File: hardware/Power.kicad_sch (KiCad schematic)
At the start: 43 parts, among them SW8 GT-TC054A-H035-L1, U10 SGM6603-ADJYN6G, U11 SGM3204, U9 AXP2101

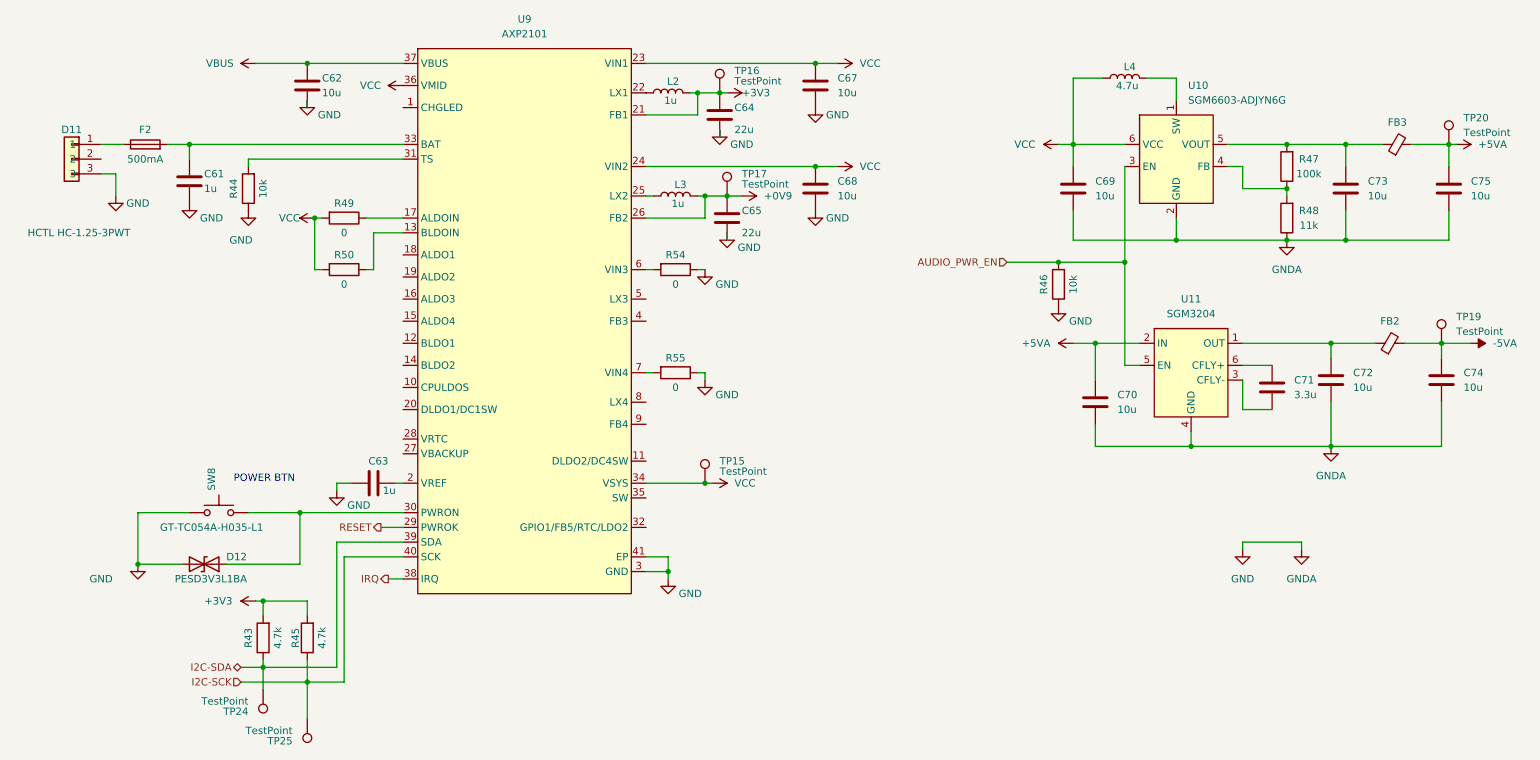
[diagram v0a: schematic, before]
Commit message: some changes on fab layers
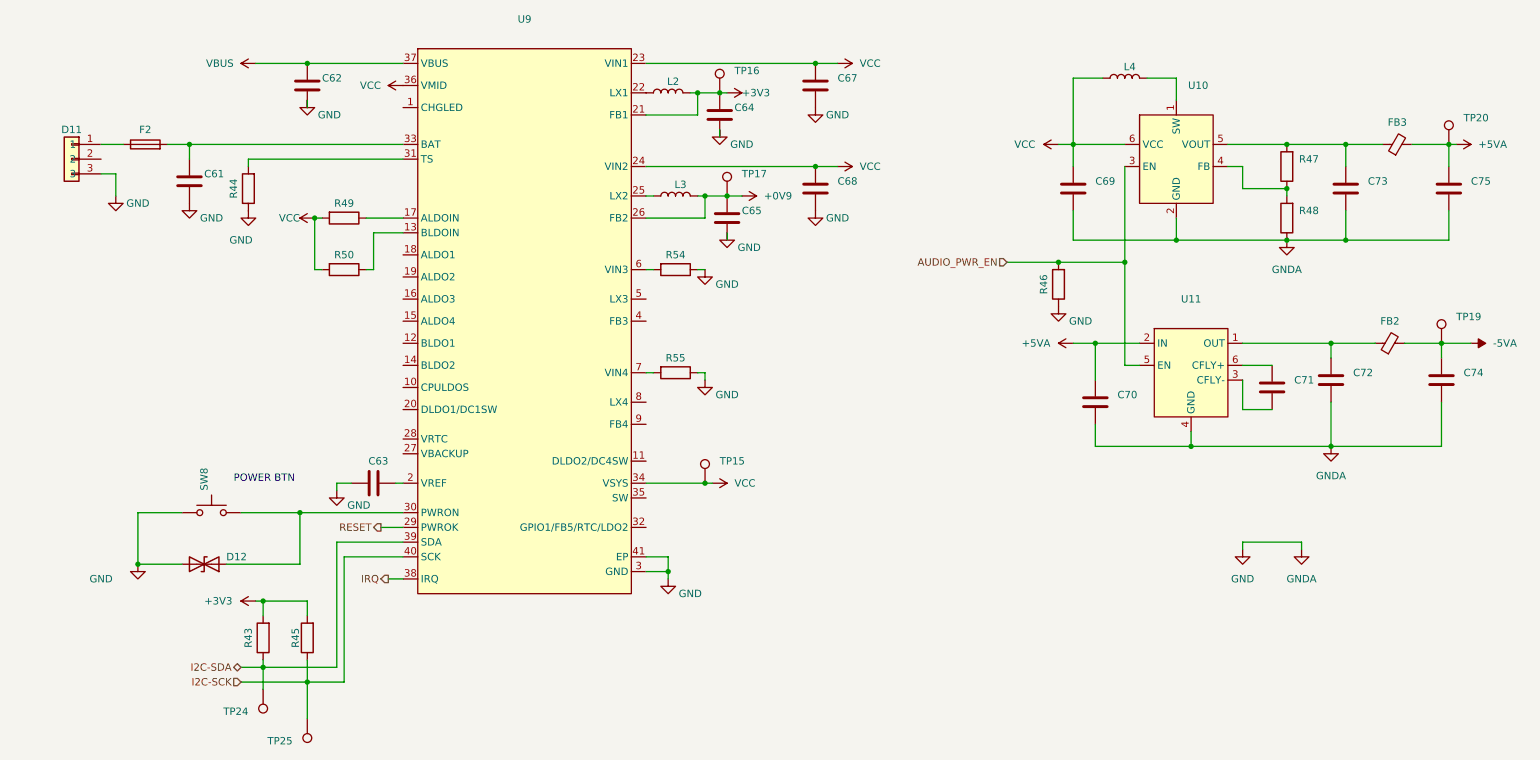
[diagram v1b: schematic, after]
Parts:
- C61, C63: value 1u -> (none); footprint rlib_passive:C_0603_1608Metric -> (none)
- C62, C67, C68, C69, C70, C72, C73, C74, C75: value 10u -> (none); footprint rlib_passive:C_0603_1608Metric -> (none)
- C64, C65: value 22u -> (none); footprint rlib_passive:C_0603_1608Metric -> (none)
- C71: value 3.3u -> (none); footprint rlib_passive:C_0603_1608Metric -> (none)
- D11: value HCTL HC-1.25-3PWT -> (none); footprint rlib_connectors:CONN-SMD_HC-1.25-3PWT -> (none)
- D12: value PESD3V3L1BA -> (none); footprint rlib_passive:D_SOD-323F -> (none)
- F2: value 500mA -> (none); footprint rlib_passive:FUSC3216X85N -> (none)
- FB2, FB3: value FerriteBead -> (none); footprint rlib_passive:INDC2520X120N -> (none)
- L2, L3: value 1u -> (none); footprint rlib_passive:INDC2016X100N -> (none)
- L4: value 4.7u -> (none); footprint rlib_passive:IND_LQH32PN4R7NN0L -> (none)
- R43, R45: value 4.7k -> (none); footprint rlib_passive:R_0603_1608Metric -> (none)
- R44, R46: value 10k -> (none); footprint rlib_passive:R_0603_1608Metric -> (none)
- R47: value 100k -> (none); footprint rlib_passive:R_0603_1608Metric -> (none)
- R48: value 11k -> (none); footprint rlib_passive:R_0603_1608Metric -> (none)
- R49, R50, R54, R55: value 0 -> (none); footprint rlib_passive:R_0603_1608Metric -> (none)
- SW8: value GT-TC054A-H035-L1 -> (none); footprint rlib_buttons:GT-TC054A-H035-L1 -> (none)
- TP15, TP16, TP17, TP19, TP20, TP24, TP25: value TestPoint -> (none); footprint TestPoint:TestPoint_Pad_D1.0mm -> (none)
- U10: value SGM6603-ADJYN6G -> (none); footprint rlib_power:SOT-23-6 -> (none)
- U11: value SGM3204 -> (none); footprint rlib_power:SOT-23-6 -> (none)
- U9: value AXP2101 -> (none); footprint rlib_power:QFN-40_L5.0-W5.0-P0.40-TL-EP3.4 -> (none)
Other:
- moved on the sheet: SW8

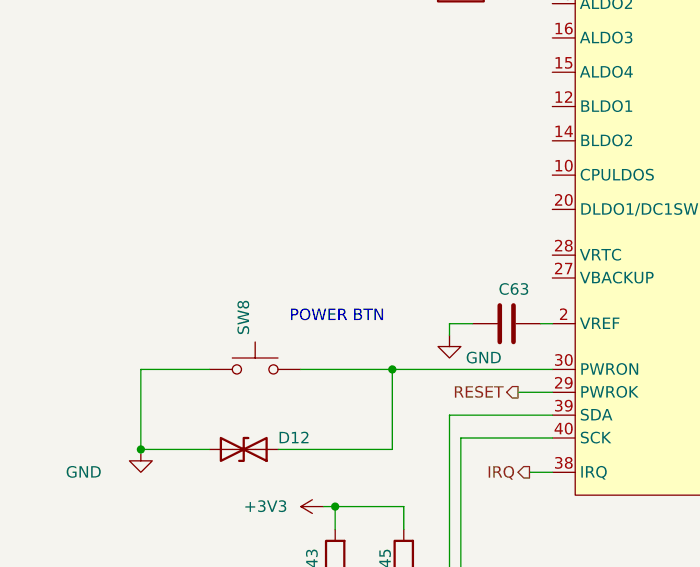
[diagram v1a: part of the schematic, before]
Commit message: pwr btn is optional connected to soc
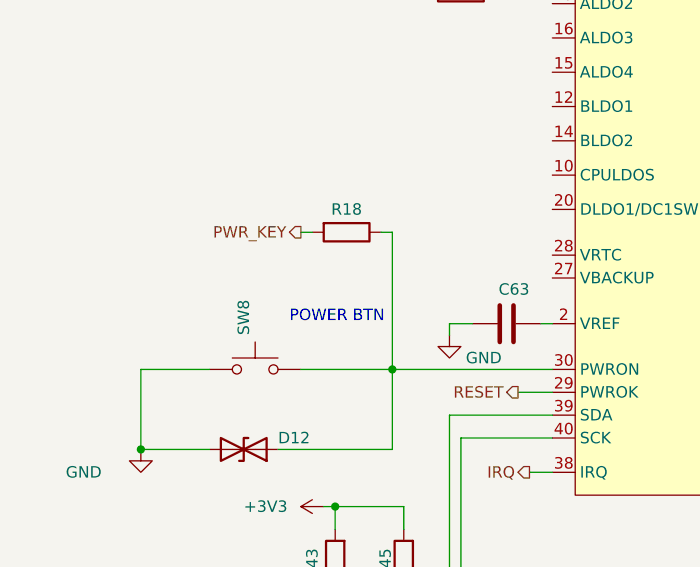
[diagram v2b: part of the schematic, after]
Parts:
- added R18: (no value), symbol rlib_passive:R
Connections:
- net at D12.1 (A1), SW8.2, U9.30 (PWRON): now also R18.1
- new net PWR_KEY: R18.2
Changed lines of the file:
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@@
+    (stroke (width 0) (type default) (color 0 0 0 0))
+  )
+  (wire (pts (xy 62.23 105.41) (xy 63.5 105.41))
     (stroke (width 0) (type default) (color 0 0 0 0))
   )
@@
     (stroke (width 0) (type default) (color 0 0 0 0))
   )
+  (wire (pts (xy 63.5 105.41) (xy 63.5 120.65))
+    (stroke (width 0) (type default) (color 0 0 0 0))
+  )
   (wire (pts (xy 132.08 48.26) (xy 132.08 52.07))
     (stroke (width 0) (type default) (color 0 0 0 0))
@@
   )
   (wire (pts (xy 214.63 49.53) (xy 214.63 45.72))
+    (stroke (width 0) (type default) (color 0 0 0 0))
+  )
+  (wire (pts (xy 53.34 105.41) (xy 54.61 105.41))
     (stroke (width 0) (type default) (color 0 0 0 0))
   )
@@
   )
   (hierarchical_label "IRQ" (shape output) (at 78.74 132.08 180)
+    (effects (font (size 1.27 1.27)) (justify right))
+  )
+  (hierarchical_label "PWR_KEY" (shape output) (at 53.34 105.41 180)
     (effects (font (size 1.27 1.27)) (justify right))
   )
@@
     (pin "1")
   )
+  (symbol (lib_id "rlib_passive:R") (at 58.42 105.41 270) (unit 1)
+    (in_bom yes) (on_board yes)
+    (property "Reference" "R18" (id 0) (at 58.42 102.87 90))
+    (property "Value" "" (id 1) (at 58.42 107.95 90))
+    (property "Footprint" "" (id 2) (at 58.42 103.632 90)
+      (effects (font (size 1.27 1.27)) hide)
+    )
+    (property "Datasheet" "~" (id 3) (at 58.42 105.41 0)
+      (effects (font (size 1.27 1.27)) hide)
+    )
+    (property "Tolerance" "" (id 4) (at 58.42 105.41 0)
+      (effects (font (size 1.27 1.27)) hide)
+    )
+    (property "Manufacturer" "Viking Tech" (id 5) (at 58.42 105.41 0)
+      (effects (font (size 1.27 1.27)) hide)
+    )
+    (property "Mnfct.  partnumber" "" (id 6) (at 58.42 105.41 0)
+      (effects (font (size 1.27 1.27)) hide)
+    )
+    (property "LCSC Partnumber" "" (id 8) (at 58.42 105.41 0)
+      (effects (font (size 1.27 1.27)) hide)
+    )
+    (property "LCSC partnumber" "C465460" (id 9) (at 58.42 105.41 0)
+      (effects (font (size 1.27 1.27)) hide)
+    )
+    (property "Mnfct. partnumber" "CR-03JA7----0R " (id 10) (at 58.42 105.41 0)
+      (effects (font (size 1.27 1.27)) hide)
+    )
+    (pin "1")
+    (pin "2")
+  )
   (symbol (lib_name "C_12") (lib_id "rlib_passive:C") (at 152.4 46.99 0) (unit 1)

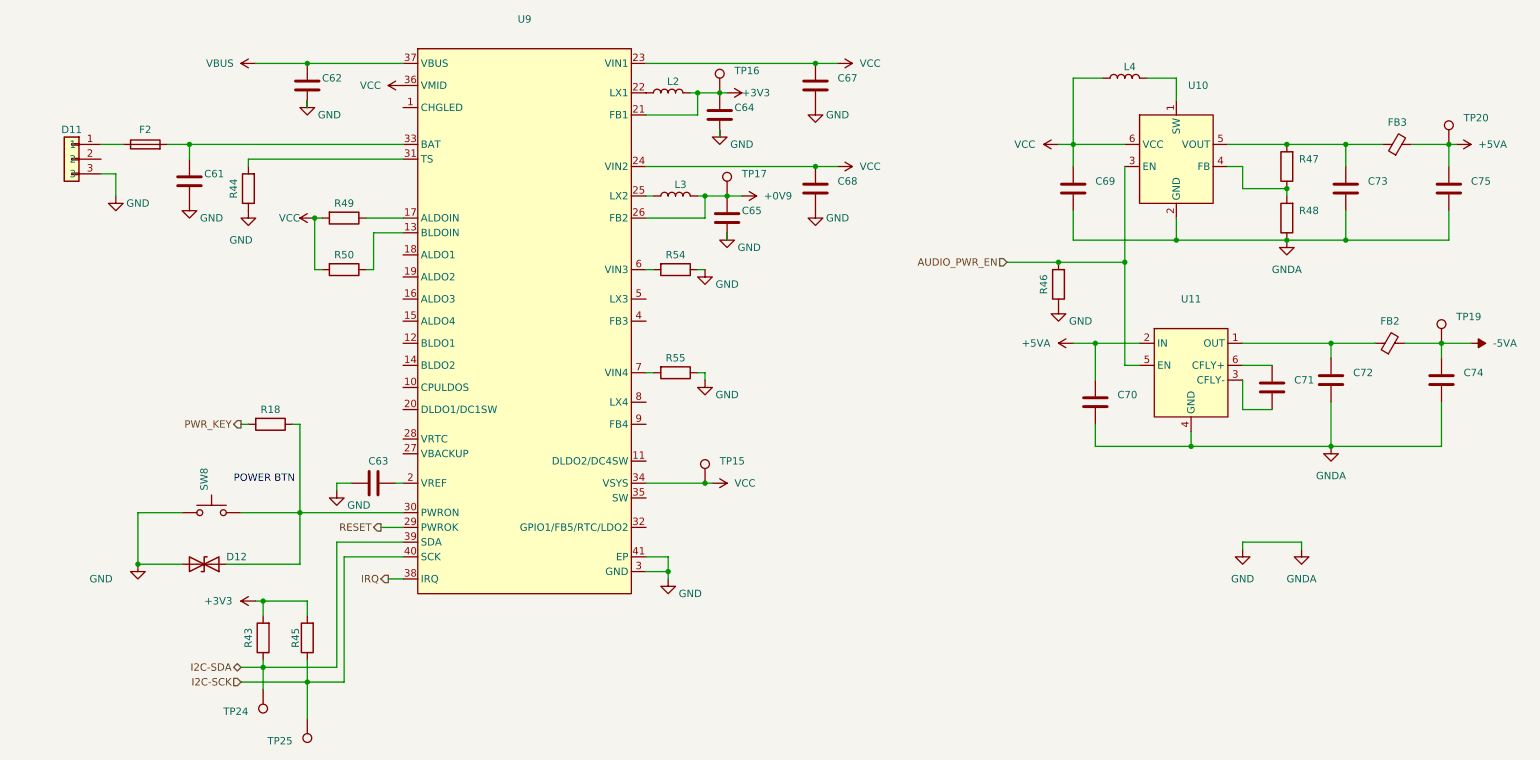
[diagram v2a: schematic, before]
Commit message: ferrite bead in adc power net is added
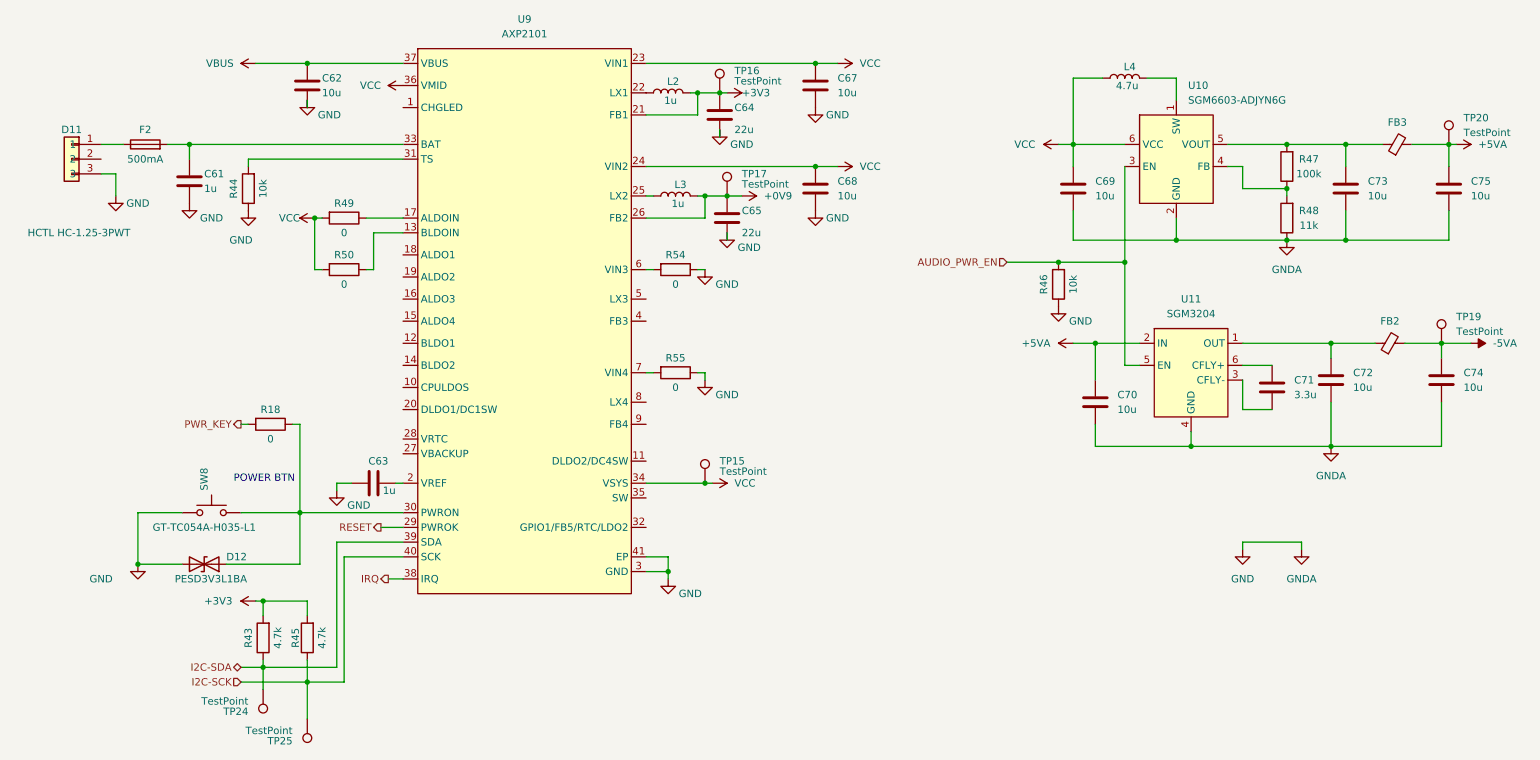
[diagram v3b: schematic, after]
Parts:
- C61, C63, L2, L3: value (none) -> 1u
- C62, C67, C68, C69, C70, C72, C73, C74, C75: value (none) -> 10u
- C64, C65: value (none) -> 22u
- C71: value (none) -> 3.3u
- D11: value (none) -> HCTL HC-1.25-3PWT
- D12: value (none) -> PESD3V3L1BA
- F2: value (none) -> 500mA
- L4: value (none) -> 4.7u
- R18, R49, R50, R54, R55: value (none) -> 0; footprint (none) -> rlib_passive:R_0603_1608Metric
- R43, R45: value (none) -> 4.7k
- R44, R46: value (none) -> 10k
- R47: value (none) -> 100k
- R48: value (none) -> 11k
- SW8: value (none) -> GT-TC054A-H035-L1
- TP15, TP16, TP17, TP19, TP20, TP24, TP25: value (none) -> TestPoint
- U10: value (none) -> SGM6603-ADJYN6G
- U11: value (none) -> SGM3204
- U9: value (none) -> AXP2101

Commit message: some fixes
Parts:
- FB2, FB3: value (none) -> FerriteBead; footprint (none) -> rlib_passive:C_0805_2012Metric
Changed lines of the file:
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@@
     (in_bom yes) (on_board yes)
     (property "Reference" "FB3" (id 0) (at 252.73 53.34 90))
-    (property "Value" "" (id 1) (at 252.6919 53.34 90)
+    (property "Value" "FerriteBead" (id 1) (at 252.6919 53.34 90)
       (effects (font (size 1.27 1.27)) hide)
     )
-    (property "Footprint" "" (id 2) (at 252.73 58.928 90)
+    (property "Footprint" "rlib_passive:C_0805_2012Metric" (id 2) (at 252.73 58.928 90)
       (effects (font (size 1.27 1.27)) hide)
     )
@@
     (in_bom yes) (on_board yes)
     (property "Reference" "FB2" (id 0) (at 251.46 87.63 90))
-    (property "Value" "" (id 1) (at 251.4219 87.63 90)
+    (property "Value" "FerriteBead" (id 1) (at 251.4219 87.63 90)
       (effects (font (size 1.27 1.27)) hide)
     )
-    (property "Footprint" "" (id 2) (at 251.46 93.218 90)
+    (property "Footprint" "rlib_passive:C_0805_2012Metric" (id 2) (at 251.46 93.218 90)
       (effects (font (size 1.27 1.27)) hide)
     )

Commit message: xxx
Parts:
- TP17: footprint (none) -> rlib_misc:TestPoint_Pad_D1.0mm
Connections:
- net at U9.20 (DLDO1/DC1SW): now also U9.27 (VBACKUP)
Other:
- moved on the sheet: R18
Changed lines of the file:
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@@
+    (stroke (width 0) (type default) (color 0 0 0 0))
+  )
+  (wire (pts (xy 81.28 110.49) (xy 77.47 110.49))
     (stroke (width 0) (type default) (color 0 0 0 0))
   )
@@
     (stroke (width 0) (type default) (color 0 0 0 0))
   )
-  (wire (pts (xy 62.23 105.41) (xy 63.5 105.41))
+  (wire (pts (xy 52.07 105.41) (xy 63.5 105.41))
     (stroke (width 0) (type default) (color 0 0 0 0))
   )
@@
     (stroke (width 0) (type default) (color 0 0 0 0))
   )
+  (wire (pts (xy 78.74 76.2) (xy 81.28 76.2))
+    (stroke (width 0) (type default) (color 0 0 0 0))
+  )
   (wire (pts (xy 123.19 43.18) (xy 152.4 43.18))
     (stroke (width 0) (type default) (color 0 0 0 0))
@@
     (stroke (width 0) (type default) (color 0 0 0 0))
   )
+  (wire (pts (xy 77.47 110.49) (xy 77.47 102.87))
+    (stroke (width 0) (type default) (color 0 0 0 0))
+  )
   (wire (pts (xy 243.84 57.15) (xy 233.68 57.15))
     (stroke (width 0) (type default) (color 0 0 0 0))
@@
     (stroke (width 0) (type default) (color 0 0 0 0))
   )
+  (wire (pts (xy 77.47 102.87) (xy 81.28 102.87))
+    (stroke (width 0) (type default) (color 0 0 0 0))
+  )
   (wire (pts (xy 78.74 132.08) (xy 81.28 132.08))
     (stroke (width 0) (type default) (color 0 0 0 0))
@@
     (stroke (width 0) (type default) (color 0 0 0 0))
   )
-  (wire (pts (xy 53.34 105.41) (xy 54.61 105.41))
+  (wire (pts (xy 43.18 105.41) (xy 44.45 105.41))
     (stroke (width 0) (type default) (color 0 0 0 0))
   )
@@
     (effects (font (size 1.27 1.27)) (justify right))
   )
-  (hierarchical_label "PWR_KEY" (shape output) (at 53.34 105.41 180)
+  (hierarchical_label "PWR_KEY" (shape output) (at 43.18 105.41 180)
     (effects (font (size 1.27 1.27)) (justify right))
   )
@@
     (pin "1")
   )
-  (symbol (lib_id "rlib_passive:R") (at 58.42 105.41 270) (unit 1)
-    (in_bom yes) (on_board yes)
-    (property "Reference" "R18" (id 0) (at 58.42 102.87 90))
-    (property "Value" "0" (id 1) (at 58.42 107.95 90))
-    (property "Footprint" "rlib_passive:R_0603_1608Metric" (id 2) (at 58.42 103.632 90)
-      (effects (font (size 1.27 1.27)) hide)
-    )
-    (property "Datasheet" "~" (id 3) (at 58.42 105.41 0)
-      (effects (font (size 1.27 1.27)) hide)
-    )
-    (property "Tolerance" "" (id 4) (at 58.42 105.41 0)
-      (effects (font (size 1.27 1.27)) hide)
-    )
-    (property "Manufacturer" "Viking Tech" (id 5) (at 58.42 105.41 0)
-      (effects (font (size 1.27 1.27)) hide)
-    )
-    (property "Mnfct.  partnumber" "" (id 6) (at 58.42 105.41 0)
-      (effects (font (size 1.27 1.27)) hide)
-    )
-    (property "LCSC Partnumber" "" (id 8) (at 58.42 105.41 0)
-      (effects (font (size 1.27 1.27)) hide)
-    )
-    (property "LCSC partnumber" "C465460" (id 9) (at 58.42 105.41 0)
-      (effects (font (size 1.27 1.27)) hide)
-    )
-    (property "Mnfct. partnumber" "CR-03JA7----0R " (id 10) (at 58.42 105.41 0)
+  (symbol (lib_id "rlib_passive:R") (at 48.26 105.41 270) (unit 1)
+    (in_bom yes) (on_board yes)
+    (property "Reference" "R18" (id 0) (at 48.26 102.87 90))
+    (property "Value" "0" (id 1) (at 48.26 107.95 90))
+    (property "Footprint" "rlib_passive:R_0603_1608Metric" (id 2) (at 48.26 103.632 90)
+      (effects (font (size 1.27 1.27)) hide)
+    )
+    (property "Datasheet" "~" (id 3) (at 48.26 105.41 0)
+      (effects (font (size 1.27 1.27)) hide)
+    )
+    (property "Tolerance" "" (id 4) (at 48.26 105.41 0)
+      (effects (font (size 1.27 1.27)) hide)
+    )
+    (property "Manufacturer" "Viking Tech" (id 5) (at 48.26 105.41 0)
+      (effects (font (size 1.27 1.27)) hide)
+    )
+    (property "Mnfct.  partnumber" "" (id 6) (at 48.26 105.41 0)
+      (effects (font (size 1.27 1.27)) hide)
+    )
+    (property "LCSC Partnumber" "" (id 8) (at 48.26 105.41 0)
+      (effects (font (size 1.27 1.27)) hide)
+    )
+    (property "LCSC partnumber" "C465460" (id 9) (at 48.26 105.41 0)
+      (effects (font (size 1.27 1.27)) hide)
+    )
+    (property "Mnfct. partnumber" "CR-03JA7----0R " (id 10) (at 48.26 105.41 0)
       (effects (font (size 1.27 1.27)) hide)
     )
@@
       (effects (font (size 1.27 1.27)) (justify left))
     )
-    (property "Footprint" "" (id 2) (at 142.24 66.04 0)
-      (effects (font (size 1.27 1.27)) hide)
-    )
+    (property "Footprint" "rlib_misc:TestPoint_Pad_D1.0mm" (id 2) (at 142.24 66.04 0)
+      (effects (font (size 1.27 1.27)) hide)
+    )
